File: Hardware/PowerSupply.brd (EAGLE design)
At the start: 45 x 37 mm, 23 parts, among them Q1 IRF730, T1 BC857, U1 MC34063

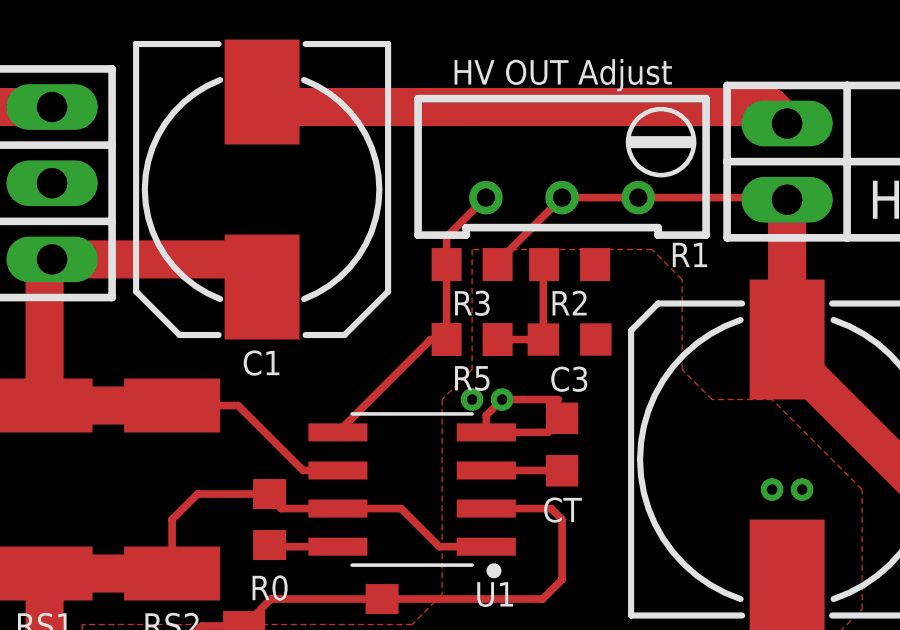
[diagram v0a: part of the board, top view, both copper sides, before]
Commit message: renamed power supply design files
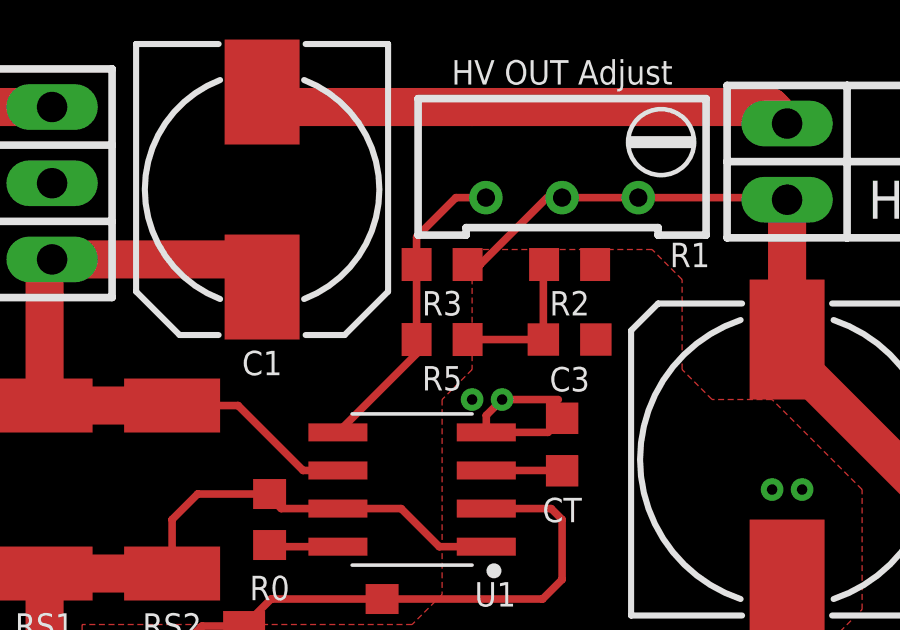
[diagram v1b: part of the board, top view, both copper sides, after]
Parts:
- C1: value 10u/16V -> 220u/16V
- C2: value 100u/16V -> 220u/16V
- moved R3 1.00 mm to (23.0, 27.5)
- moved R5 1.00 mm to (23.0, 25.0)
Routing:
- net N$7: track 4.04 -> 5.04 mm
- net V+: track 32.3 -> 33.3 mm
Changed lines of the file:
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@@
 <layer number="14" name="Route14" color="22" fill="1" visible="no" active="no"/>
 <layer number="15" name="Route15" color="23" fill="1" visible="no" active="no"/>
-<layer number="16" name="Bottom" color="1" fill="1" visible="no" active="yes"/>
+<layer number="16" name="Bottom" color="1" fill="1" visible="yes" active="yes"/>
 <layer number="17" name="Pads" color="2" fill="1" visible="yes" active="yes"/>
 <layer number="18" name="Vias" color="2" fill="1" visible="yes" active="yes"/>
@@
 <layer number="20" name="Dimension" color="24" fill="1" visible="yes" active="yes"/>
 <layer number="21" name="tPlace" color="7" fill="1" visible="yes" active="yes"/>
-<layer number="22" name="bPlace" color="7" fill="1" visible="no" active="yes"/>
+<layer number="22" name="bPlace" color="7" fill="1" visible="yes" active="yes"/>
 <layer number="23" name="tOrigins" color="15" fill="1" visible="yes" active="yes"/>
-<layer number="24" name="bOrigins" color="15" fill="1" visible="no" active="yes"/>
+<layer number="24" name="bOrigins" color="15" fill="1" visible="yes" active="yes"/>
 <layer number="25" name="tNames" color="7" fill="1" visible="yes" active="yes"/>
-<layer number="26" name="bNames" color="7" fill="1" visible="no" active="yes"/>
+<layer number="26" name="bNames" color="7" fill="1" visible="yes" active="yes"/>
 <layer number="27" name="tValues" color="7" fill="1" visible="no" active="yes"/>
 <layer number="28" name="bValues" color="7" fill="1" visible="no" active="yes"/>
@@
 <layer number="38" name="bTest" color="7" fill="1" visible="no" active="yes"/>
 <layer number="39" name="tKeepout" color="4" fill="11" visible="yes" active="yes"/>
-<layer number="40" name="bKeepout" color="1" fill="11" visible="no" active="yes"/>
+<layer number="40" name="bKeepout" color="1" fill="11" visible="yes" active="yes"/>
 <layer number="41" name="tRestrict" color="4" fill="10" visible="yes" active="yes"/>
-<layer number="42" name="bRestrict" color="1" fill="10" visible="no" active="yes"/>
+<layer number="42" name="bRestrict" color="1" fill="10" visible="yes" active="yes"/>
 <layer number="43" name="vRestrict" color="2" fill="10" visible="no" active="yes"/>
 <layer number="44" name="Drills" color="7" fill="1" visible="no" active="yes"/>
@@
 <layer number="50" name="dxf" color="7" fill="1" visible="no" active="no"/>
 <layer number="51" name="tDocu" color="7" fill="1" visible="yes" active="yes"/>
-<layer number="52" name="bDocu" color="7" fill="1" visible="no" active="yes"/>
+<layer number="52" name="bDocu" color="7" fill="1" visible="yes" active="yes"/>
 <layer number="53" name="tGND_GNDA" color="7" fill="9" visible="no" active="no"/>
 <layer number="54" name="bGND_GNDA" color="1" fill="9" visible="no" active="no"/>
@@
 </autorouter>
 <elements>
-<element name="C1" library="rcl" library_urn="urn:adsk.eagle:library:334" package="140CLH-0810" package3d_urn="urn:adsk.eagle:package:23392/1" value="10u/16V" x="17" y="30" smashed="yes" rot="R270">
+<element name="C1" library="rcl" library_urn="urn:adsk.eagle:library:334" package="140CLH-0810" package3d_urn="urn:adsk.eagle:package:23392/1" value="220u/16V" x="17" y="30" smashed="yes" rot="R270">
 <attribute name="NAME" x="17" y="24.623" size="0.8128" layer="25" font="vector" align="top-center"/>
 <attribute name="SPICEPREFIX" value="C" x="-16.02" y="10.95" size="1.778" layer="27" rot="R270" display="off"/>
@@
 <element name="U1" library="NixieClock" library_urn="urn:adsk.eagle:library:7479626" package="SOIC127P600X175-8" package3d_urn="urn:adsk.eagle:package:7646370/1" value="MC34063" x="22" y="20" smashed="yes" rot="R180">
 <attribute name="NAME" x="25.45765" y="16.9131" size="0.8128" layer="25" font="vector" align="top-right"/>
+<attribute name="SPICEPREFIX" value="X" x="22" y="20" size="1.778" layer="27" rot="R180" display="off"/>
 <attribute name="VALUE" x="22" y="23.1549" size="1.27" layer="27" rot="R180" align="top-center"/>
 </element>
@@
 <element name="Q1" library="transistor-power" library_urn="urn:adsk.eagle:library:400" package="TO220BV" package3d_urn="urn:adsk.eagle:package:29484/3" value="IRF730" x="16.5" y="9" smashed="yes">
 <attribute name="NAME" x="16.5" y="9.127" size="0.8128" layer="25" font="vector" ratio="10" align="bottom-center"/>
+<attribute name="SPICEPREFIX" value="Q" x="16.5" y="9" size="1.778" layer="27" display="off"/>
 <attribute name="VALUE" x="11.42" y="1.38" size="1.27" layer="27" ratio="10"/>
 </element>
-<element name="C2" library="rcl" library_urn="urn:adsk.eagle:library:334" package="140CLH-0810" package3d_urn="urn:adsk.eagle:package:23392/1" value="100u/16V" x="6" y="6.5" smashed="yes" rot="R270">
+<element name="C2" library="rcl" library_urn="urn:adsk.eagle:library:334" package="140CLH-0810" package3d_urn="urn:adsk.eagle:package:23392/1" value="220u/16V" x="6" y="6.5" smashed="yes" rot="R270">
 <attribute name="NAME" x="6" y="11.877" size="0.8128" layer="25" font="vector" align="bottom-center"/>
 <attribute name="SPICEPREFIX" value="C" x="6" y="6.5" size="1.778" layer="27" rot="R270" display="off"/>
@@
 <element name="U$1" library="NixieClock" library_urn="urn:adsk.eagle:library:7479626" package="SIGN-HV" package3d_urn="urn:adsk.eagle:package:7683982/2" value="" x="31" y="15" smashed="yes" rot="MR0"/>
 <element name="U$2" library="OwnStuff" library_urn="urn:adsk.eagle:library:2060095" package="LOGO-SILKSCREEN" package3d_urn="urn:adsk.eagle:package:2060168/1" value="" x="11" y="21" smashed="yes" rot="MR0"/>
-<element name="R3" library="rcl" library_urn="urn:adsk.eagle:library:334" package="R0603" package3d_urn="urn:adsk.eagle:package:23555/2" value="DNP" x="24" y="27.5" smashed="yes" rot="R180">
-<attribute name="NAME" x="24" y="26.6146" size="0.8128" layer="25" font="vector" align="top-center"/>
-<attribute name="SPICEPREFIX" value="R" x="24" y="27.5" size="1.778" layer="27" rot="R180" display="off"/>
-<attribute name="VALUE" x="25.4984" y="26.3646" size="1.27" layer="27" align="top-right"/>
-</element>
-<element name="R5" library="rcl" library_urn="urn:adsk.eagle:library:334" package="R0603" package3d_urn="urn:adsk.eagle:package:23555/2" value="0R" x="24" y="25" smashed="yes">
-<attribute name="NAME" x="24" y="24.1146" size="0.8128" layer="25" font="vector" align="top-center"/>
-<attribute name="SPICEPREFIX" value="R" x="24" y="25" size="1.778" layer="27" display="off"/>
-<attribute name="VALUE" x="25.4984" y="23.8646" size="1.27" layer="27" align="top-right"/>
+<element name="R3" library="rcl" library_urn="urn:adsk.eagle:library:334" package="R0603" package3d_urn="urn:adsk.eagle:package:23555/2" value="DNP" x="23" y="27.5" smashed="yes" rot="R180">
+<attribute name="NAME" x="23" y="26.6146" size="0.8128" layer="25" font="vector" align="top-center"/>
+<attribute name="SPICEPREFIX" value="R" x="23" y="27.5" size="1.778" layer="27" rot="R180" display="off"/>
+<attribute name="VALUE" x="24.4984" y="26.3646" size="1.27" layer="27" align="top-right"/>
+</element>
+<element name="R5" library="rcl" library_urn="urn:adsk.eagle:library:334" package="R0603" package3d_urn="urn:adsk.eagle:package:23555/2" value="0R" x="23" y="25" smashed="yes">
+<attribute name="NAME" x="23" y="24.1146" size="0.8128" layer="25" font="vector" align="top-center"/>
+<attribute name="SPICEPREFIX" value="R" x="23" y="25" size="1.778" layer="27" display="off"/>
+<attribute name="VALUE" x="24.4984" y="23.8646" size="1.27" layer="27" align="top-right"/>
 </element>
 </elements>
@@
 <wire x1="29.54" y1="29.73" x2="34.43" y2="29.73" width="0.254" layer="1"/>
 <wire x1="34.43" y1="29.73" x2="34.5" y2="29.66" width="0.254" layer="1"/>
-<wire x1="27" y1="29.73" x2="24.85" y2="27.58" width="0.254" layer="1"/>
-<wire x1="24.85" y1="27.58" x2="24.85" y2="27.5" width="0.254" layer="1"/>
+<wire x1="27" y1="29.73" x2="26.5" y2="29.73" width="0.254" layer="1"/>
+<wire x1="26.5" y1="29.73" x2="24.27" y2="27.5" width="0.254" layer="1"/>
+<wire x1="24.27" y1="27.5" x2="23.85" y2="27.5" width="0.254" layer="1"/>
 </signal>
 <signal name="+12V">
@@
 <contactref element="C3" pad="1"/>
 <contactref element="R5" pad="2"/>
-<wire x1="26.375" y1="25" x2="24.85" y2="25" width="0.254" layer="1"/>
+<wire x1="26.375" y1="25" x2="23.85" y2="25" width="0.254" layer="1"/>
 <wire x1="26.4" y1="27.5" x2="26.375" y2="27.475" width="0.254" layer="1"/>
 <wire x1="26.375" y1="27.475" x2="26.375" y2="25" width="0.254" layer="1"/>
@@
 <contactref element="R1" pad="1"/>
 <contactref element="R3" pad="2"/>
-<wire x1="23.15" y1="25" x2="23.15" y2="27.5" width="0.254" layer="1"/>
-<wire x1="23.15" y1="27.5" x2="23.15" y2="28.42" width="0.254" layer="1"/>
-<wire x1="23.15" y1="28.42" x2="24.46" y2="29.73" width="0.254" layer="1"/>
-<wire x1="19.5266" y1="21.905" x2="22.6216" y2="25" width="0.254" layer="1"/>
-<wire x1="22.6216" y1="25" x2="23.15" y2="25" width="0.254" layer="1"/>
+<wire x1="22.15" y1="27.5" x2="22.15" y2="25" width="0.254" layer="1"/>
+<wire x1="23.46" y1="29.73" x2="22.15" y2="28.42" width="0.254" layer="1"/>
+<wire x1="22.15" y1="27.5" x2="22.15" y2="28.42" width="0.254" layer="1"/>
+<wire x1="23.46" y1="29.73" x2="24.46" y2="29.73" width="0.254" layer="1"/>
+<wire x1="19.5266" y1="21.905" x2="22.15" y2="24.5284" width="0.254" layer="1"/>
+<wire x1="22.15" y1="24.5284" x2="22.15" y2="25" width="0.254" layer="1"/>
 </signal>
 </signals>
